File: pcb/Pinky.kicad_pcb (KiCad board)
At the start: 2 copper layers, 142.2 x 120.5 mm, 80 parts, among them J1 MJ-4PP-9, P1 i2c-pin, P2 i2c-pin, SW1 RESET_SW, SW10 SW_PUSH, SW11 SW_PUSH, SW12 SW_PUSH, SW13 SW_PUSH, SW14 SW_PUSH, SW15 SW_PUSH, SW16 SW_PUSH, SW17 SW_PUSH, SW18 SW_PUSH, SW19 SW_PUSH, SW2 SW_PUSH, SW20 SW_PUSH, SW21 SW_PUSH, SW22 SW_PUSH, SW23 SW_PUSH, SW24 SW_PUSH, SW25 SW_PUSH, SW26 SW_PUSH, SW27 SW_PUSH, SW28 SW_PUSH, SW29 SW_PUSH, SW3 SW_PUSH, SW30 SW_PUSH, SW31 SW_PUSH, SW32 SW_PUSH, SW33 SW_PUSH, SW4 SW_PUSH, SW5 SW_PUSH, SW6 SW_PUSH, SW7 SW_PUSH, SW8 SW_PUSH, SW9 SW_PUSH, U1 ProMicro

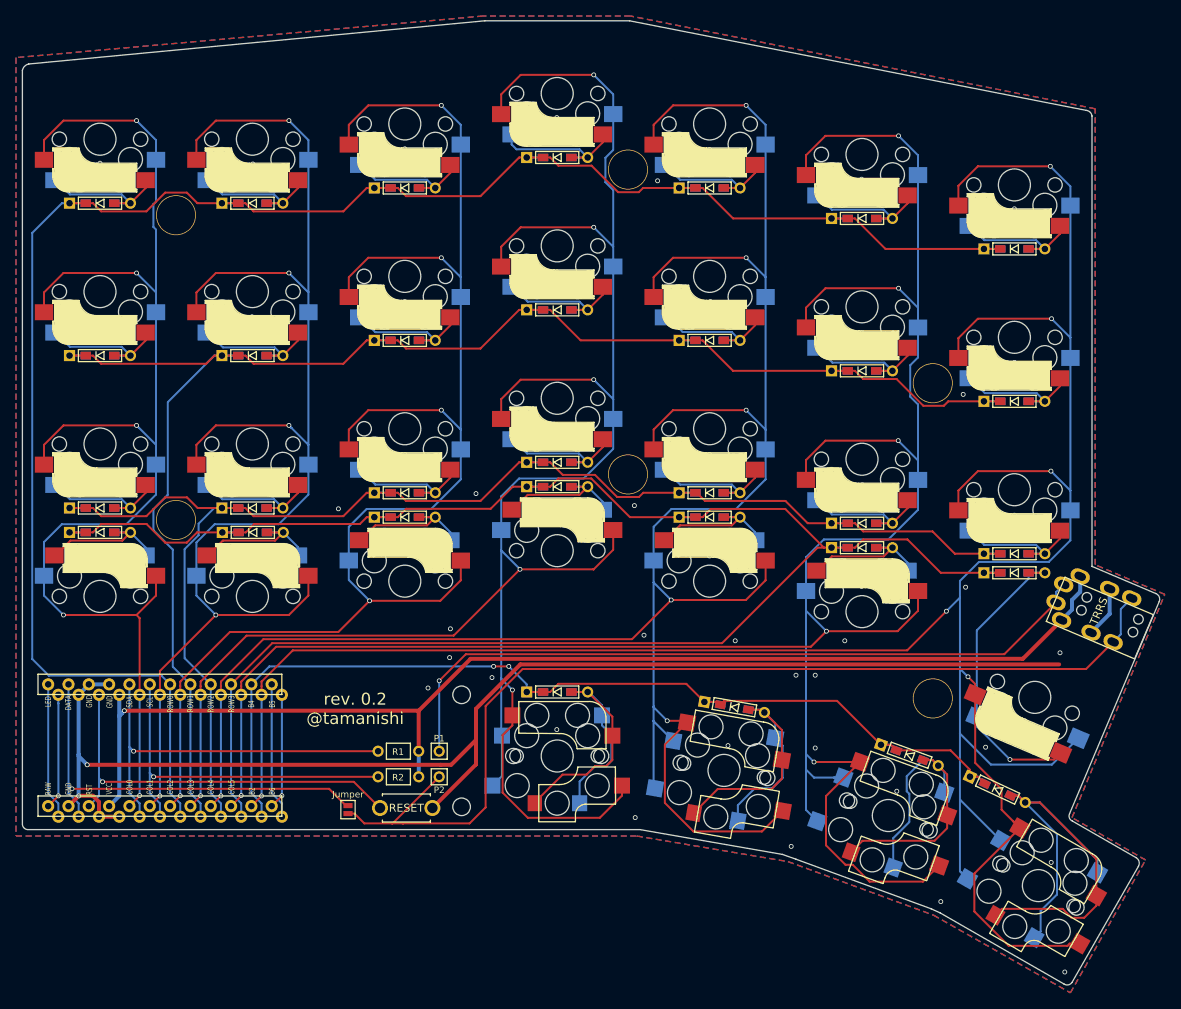
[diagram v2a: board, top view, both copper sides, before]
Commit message: move thumb keys inside
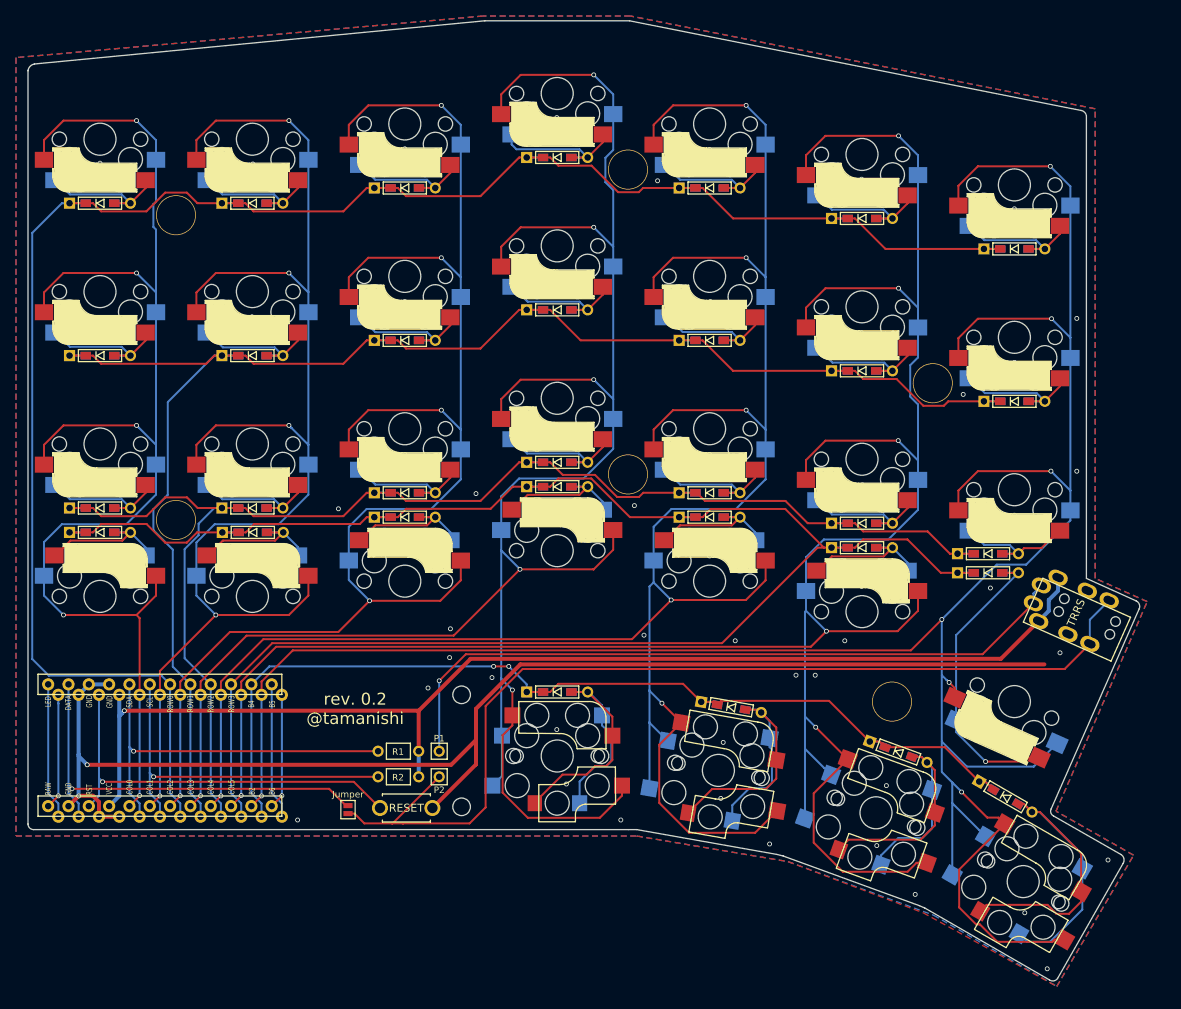
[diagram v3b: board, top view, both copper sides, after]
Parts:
- moved Ref** 3.55 mm to (149.0, 120.3)
- moved D30 3.30 mm to (161.0, 101.8)
- moved D31 3.30 mm to (161.0, 104.2)
- moved J1 2.92 mm to (177.6, 112.5), turned to 246 degrees
- moved SW32 2.60 mm to (164.3, 120.3), turned to 156 degrees
- moved SW33 1.96 mm to (165.4, 142.8)
- moved SW28 1.58 mm to (147.0, 134.2)
- moved D27 1.46 mm to (149.8, 126.6)
- moved D32 1.35 mm to (163.2, 132.2), turned to 330 degrees
- moved SW23 0.70 mm to (127.3, 128.9)
- moved D22 0.40 mm to (128.9, 121.0)
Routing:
- net col6: track 337.5 -> 318.1 mm, vias 6 -> 7
- net Net-(D32-Pad2): track 69.6 -> 58.1 mm
- net GND: track 174.0 -> 165.7 mm, vias 56 -> 60
- net row3: track 240.1 -> 236.8 mm
- net row2: track 185.0 -> 181.7 mm
- net Net-(J1-PadB): track 127.8 -> 124.8 mm
- net VCC: track 152.0 -> 149.0 mm
- net Net-(J1-PadA): track 92.6 -> 89.7 mm
- net Net-(D22-Pad2): track 45.8 -> 43.6 mm
- net col5: track 302.5 -> 300.7 mm
- net Net-(D27-Pad2): track 45.0 -> 43.4 mm
- net col4: track 281.0 -> 282.2 mm
- net row4: track 126.6 -> 127.5 mm
- net Net-(D31-Pad2): track 38.7 -> 39.4 mm
- net Net-(D30-Pad2): track 18.4 -> 17.9 mm
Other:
- board size 142.2 x 120.5 mm -> 139 x 120 mm
